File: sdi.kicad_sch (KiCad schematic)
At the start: 42 parts, among them J12 0875-1G2T-V5, U2 DP83849CVS_NOPB, X1 CB3LV-3I-25M0000

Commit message: Finish Regulator section
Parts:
- renumbered C40 to C37, C11 to C39, C34 to C40, C35 to C41, C36 to C42, C37 to C43, C39 to C45, C9 to C51, C10 to C53, C5 to C54, C6 to C56, C7 to C59, C8 to C60, C1 to C63, C3 to C64, C2 to C70, C4 to C71, J12 to J8, L3 to L20, L4 to L21, R6 to R100, R17 to R101, R15 to R102, R3 to R105, R11 to R106, R4 to R107, R12 to R108, R18 to R109, R16 to R110, R14 to R113, R13 to R114, R19 to R115, R20 to R116, R24 to R87, R21 to R94, R22 to R95, R23 to R96, R1 to R97, R5 to R98, R2 to R99, U2 to U6

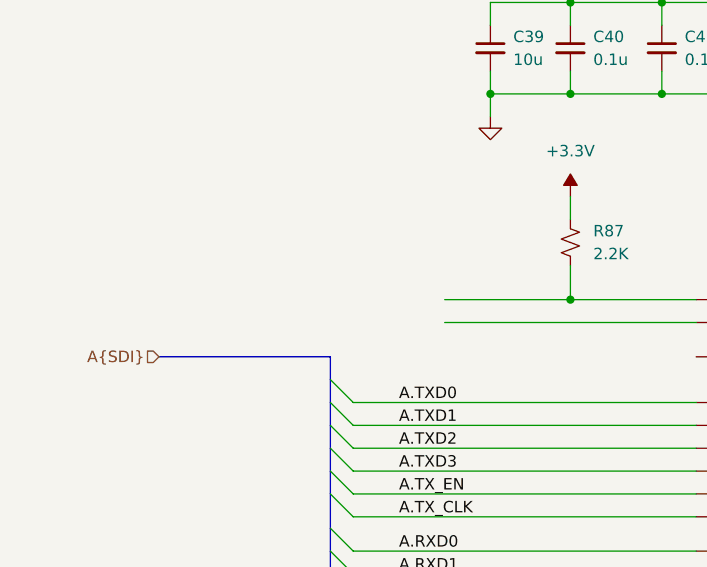
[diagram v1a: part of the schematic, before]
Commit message: Place SFP passives
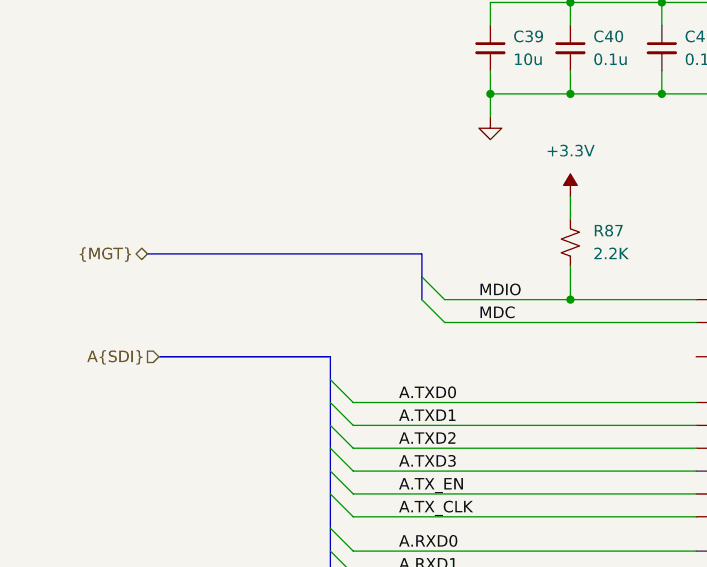
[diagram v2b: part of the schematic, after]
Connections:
- net MDIO: now reaches R87.2, U6.66 (MDIO)
- net MDC: now reaches U6.67 (MDC)
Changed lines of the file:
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@@
 	(generator_version "9.0")
 	(paper "B")
+	(bus_alias "MGT"
+		(members "MDIO" "MDC")
+	)
 	(bus_alias "SDI"
 		(members "TXD0" "TXD1" "TXD2" "TXD3" "TX_EN" "TX_CLK" "RXD0" "RXD1" "RXD2"
@@
 	)
 	(bus_entry
+		(at 85.09 72.39)
+		(size 2.54 2.54)
+		(stroke
+			(width 0)
+			(type default)
+		)
+	)
+	(bus_entry
 		(at 74.93 153.67)
 		(size 2.54 2.54)
@@
 	)
 	(bus_entry
+		(at 85.09 69.85)
+		(size 2.54 2.54)
+		(stroke
+			(width 0)
+			(type default)
+		)
+	)
+	(bus_entry
 		(at 74.93 97.79)
 		(size 2.54 2.54)
@@
 		)
 	)
+	(bus
+		(pts
+			(xy 54.61 67.31) (xy 85.09 67.31)
+		)
+		(stroke
+			(width 0)
+			(type default)
+		)
+	)
 	(wire
 		(pts
@@
 		)
 	)
+	(bus
+		(pts
+			(xy 85.09 72.39) (xy 85.09 69.85)
+		)
+		(stroke
+			(width 0)
+			(type default)
+		)
+	)
 	(wire
 		(pts
@@
 		)
 	)
+	(bus
+		(pts
+			(xy 85.09 69.85) (xy 85.09 67.31)
+		)
+		(stroke
+			(width 0)
+			(type default)
+		)
+	)
 	(wire
 		(pts
@@
 		)
 	)
+	(label "MDIO"
+		(at 91.44 72.39 0)
+		(effects
+			(font
+				(size 1.27 1.27)
+			)
+			(justify left bottom)
+		)
+	)
 	(label "B.TXD0"
 		(at 82.55 127 0)
@@
 		)
 	)
+	(label "MDC"
+		(at 91.44 74.93 0)
+		(effects
+			(font
+				(size 1.27 1.27)
+			)
+			(justify left bottom)
+		)
+	)
 	(label "A.TXD0"
 		(at 82.55 83.82 0)
@@
 		(effects
 			(font
+				(size 1.27 1.27)
+			)
+			(justify right)
+		)
+	)
+	(hierarchical_label "{MGT}"
+		(shape bidirectional)
+		(at 54.61 67.31 180)
+		(effects
+			(font
